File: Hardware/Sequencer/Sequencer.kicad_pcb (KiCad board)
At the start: 2 copper layers, 200 x 130 mm, 37 parts, among them J301 Conn_ST_STDC14, J601 USB_C_Receptacle_USB2.0_16P, SW301 SW_Push, SW401 SW_SP4T_NR01104, SW402 SW_SP4T_NR01104, SW403 SW_SP4T_NR01104, U301 STM32G474RETx, U401 MCP23017_SP, U402 MCP23017_SP, U601 USBLC6-2SC6, U602 AZ1117-3.3TRG1

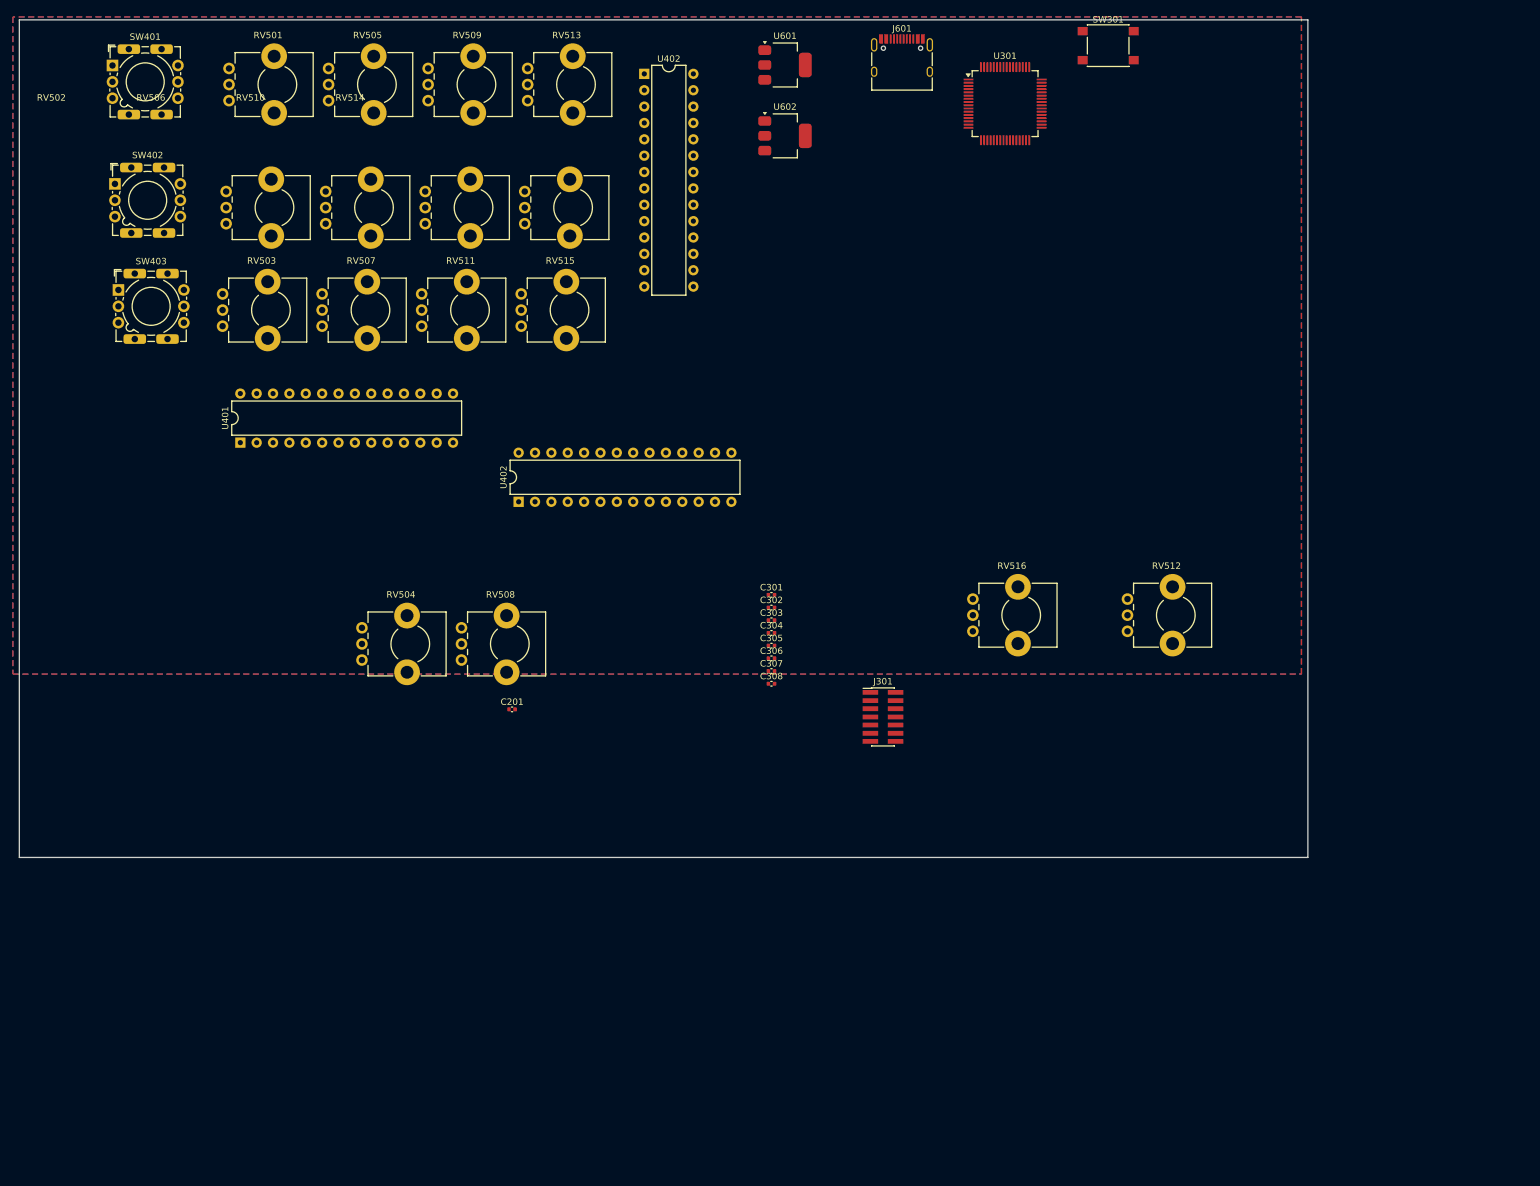
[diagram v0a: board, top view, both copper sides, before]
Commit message: update dimension pcb, footprint
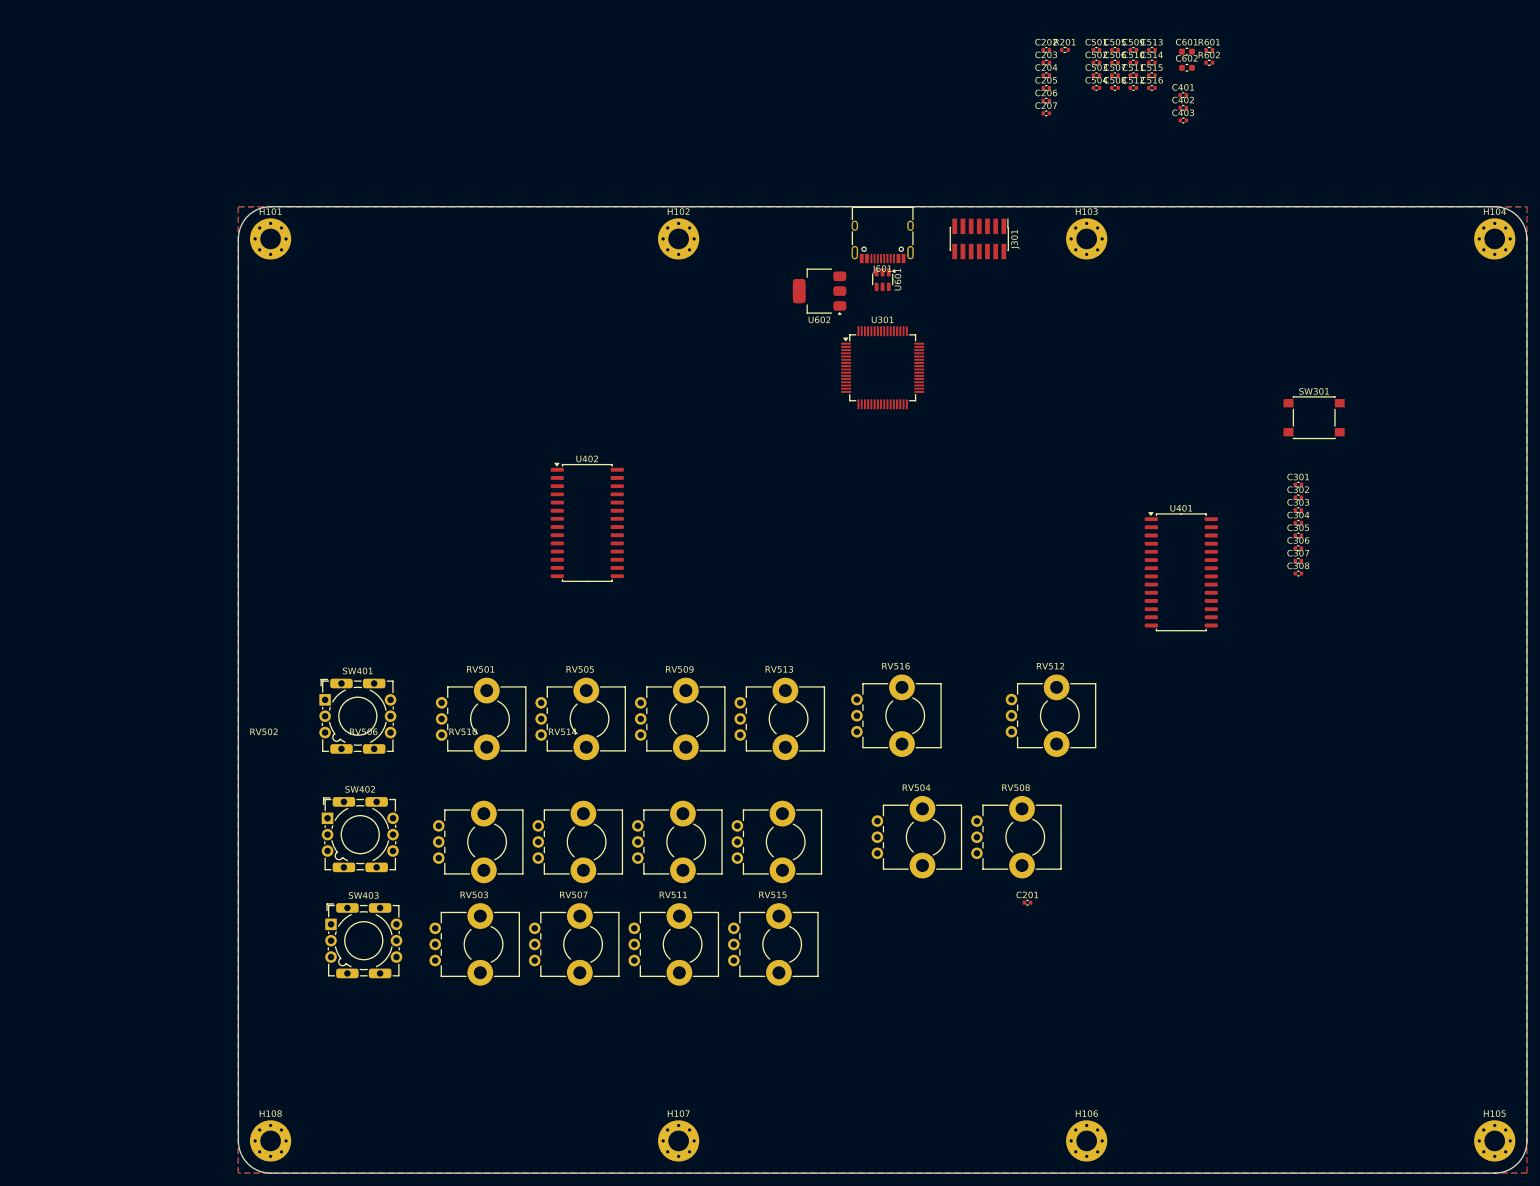
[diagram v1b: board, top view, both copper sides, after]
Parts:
- removed the U402 at (143.5, 95.8)
- added C202: 10n, Capacitor_SMD:C_0402_1005Metric, F.Cu at (225.4, 25.7)
- added C203: 1n, Capacitor_SMD:C_0402_1005Metric, F.Cu at (225.4, 27.6)
- added C204: 1n, Capacitor_SMD:C_0402_1005Metric, F.Cu at (225.4, 29.6)
- added C205: 1u, Capacitor_SMD:C_0402_1005Metric, F.Cu at (225.4, 31.6)
- added C206: 10n, Capacitor_SMD:C_0402_1005Metric, F.Cu at (225.4, 33.5)
- added C207: 1u, Capacitor_SMD:C_0402_1005Metric, F.Cu at (225.4, 35.5)
- added C401: 10n, Capacitor_SMD:C_0402_1005Metric, F.Cu at (246.7, 32.7)
- added C402: 10n, Capacitor_SMD:C_0402_1005Metric, F.Cu at (246.7, 34.6)
- added C403: 10n, Capacitor_SMD:C_0402_1005Metric, F.Cu at (246.7, 36.6)
- added C501: 10n, Capacitor_SMD:C_0402_1005Metric, F.Cu at (233.2, 25.7)
- added C502: 10n, Capacitor_SMD:C_0402_1005Metric, F.Cu at (233.2, 27.6)
- added C503: 10n, Capacitor_SMD:C_0402_1005Metric, F.Cu at (233.2, 29.6)
- added C504: 10n, Capacitor_SMD:C_0402_1005Metric, F.Cu at (233.2, 31.6)
- added C505: 10n, Capacitor_SMD:C_0402_1005Metric, F.Cu at (236.1, 25.7)
- added C506: 10n, Capacitor_SMD:C_0402_1005Metric, F.Cu at (236.1, 27.6)
- added C507: 10n, Capacitor_SMD:C_0402_1005Metric, F.Cu at (236.1, 29.6)
- added C508: 10n, Capacitor_SMD:C_0402_1005Metric, F.Cu at (236.1, 31.6)
- added C509: 10n, Capacitor_SMD:C_0402_1005Metric, F.Cu at (238.9, 25.7)
- added C510: 10n, Capacitor_SMD:C_0402_1005Metric, F.Cu at (238.9, 27.6)
- added C511: 10n, Capacitor_SMD:C_0402_1005Metric, F.Cu at (238.9, 29.6)
- added C512: 10n, Capacitor_SMD:C_0402_1005Metric, F.Cu at (238.9, 31.6)
- added C513: 10n, Capacitor_SMD:C_0402_1005Metric, F.Cu at (241.8, 25.7)
- added C514: 10n, Capacitor_SMD:C_0402_1005Metric, F.Cu at (241.8, 27.6)
- added C515: 10n, Capacitor_SMD:C_0402_1005Metric, F.Cu at (241.8, 29.6)
- added C516: 10n, Capacitor_SMD:C_0402_1005Metric, F.Cu at (241.8, 31.6)
- added C601: 10u, Capacitor_SMD:C_0603_1608Metric, F.Cu at (247.2, 25.9)
- added C602: 22u, Capacitor_SMD:C_0603_1608Metric, F.Cu at (247.2, 28.4)
- added H101: MountingHole_Pad, MountingHole:MountingHole_3.2mm_M3_Pad_Via, F.Cu at (105.0, 55.0)
- added H102: MountingHole_Pad, MountingHole:MountingHole_3.2mm_M3_Pad_Via, F.Cu at (168.3, 55.0)
- added H103: MountingHole_Pad, MountingHole:MountingHole_3.2mm_M3_Pad_Via, F.Cu at (231.7, 55.0)
- added H104: MountingHole_Pad, MountingHole:MountingHole_3.2mm_M3_Pad_Via, F.Cu at (295.0, 55.0)
- added H105: MountingHole_Pad, MountingHole:MountingHole_3.2mm_M3_Pad_Via, F.Cu at (295.0, 195.0)
- added H106: MountingHole_Pad, MountingHole:MountingHole_3.2mm_M3_Pad_Via, F.Cu at (231.7, 195.0)
- added H107: MountingHole_Pad, MountingHole:MountingHole_3.2mm_M3_Pad_Via, F.Cu at (168.3, 195.0)
- added H108: MountingHole_Pad, MountingHole:MountingHole_3.2mm_M3_Pad_Via, F.Cu at (105.0, 195.0)
- added R201: 1k, Resistor_SMD:R_0402_1005Metric, F.Cu at (228.3, 25.7)
- added R601: 5k1, Resistor_SMD:R_0402_1005Metric, F.Cu at (250.7, 25.7)
- added R602: 5k1, Resistor_SMD:R_0402_1005Metric, F.Cu at (250.7, 27.7)
- U401, U402: footprint Package_DIP:DIP-28_W7.62mm -> Package_SO:SOIC-28W_7.5x17.9mm_P1.27mm
- U601: footprint Package_TO_SOT_SMD:SOT-223-3_TabPin2 -> Package_TO_SOT_SMD:SOT-23-6
- moved U401 147.4 mm to (246.3, 106.7), turned to 0 degrees
- moved RV501 103.8 mm to (131.6, 132.0)
- moved RV505 103.8 mm to (147.0, 132.0)
- moved RV509 103.8 mm to (162.4, 132.0)
- moved RV513 103.8 mm to (177.9, 132.0)
- moved SW401 103.8 mm to (113.5, 126.5)
- moved RV502 103.8 mm to (131.1, 151.1)
- moved RV503 103.8 mm to (130.6, 167.0)
- moved RV506 103.8 mm to (146.6, 151.1)
- moved RV507 103.8 mm to (146.0, 167.0)
- moved RV510 103.8 mm to (162.0, 151.1)
- moved RV511 103.8 mm to (161.4, 167.0)
- moved RV514 103.8 mm to (177.4, 151.1)
- moved RV515 103.8 mm to (176.9, 167.0)
- moved SW403 103.8 mm to (114.4, 161.4)
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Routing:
- added copper zone on B.Cu, net GND
- added copper zone on F.Cu, net GND
- removed copper zone on B.Cu, net (none)
- removed copper zone on F.Cu, net (none)
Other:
- board size 200 x 130 mm -> 200 x 150 mm

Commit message: pcb
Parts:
- added C1: 100n, Capacitor_SMD:C_0402_1005Metric, B.Cu at (254.6, 137.1)
- added C10: 100n, Capacitor_SMD:C_0402_1005Metric, B.Cu at (134.2, 171.0)
- added C11: 100n, Capacitor_SMD:C_0402_1005Metric, F.Cu at (156.6, 166.1)
- added C12: 100n, Capacitor_SMD:C_0402_1005Metric, F.Cu at (176.6, 166.1)
- added C13: 100n, Capacitor_SMD:C_0402_1005Metric, F.Cu at (196.6, 166.1)
- added C14: 100n, Capacitor_SMD:C_0402_1005Metric, F.Cu at (216.6, 166.1)
- added C15: 100n, Capacitor_SMD:C_0402_1005Metric, F.Cu at (236.6, 166.1)
- added C16: 100n, Capacitor_SMD:C_0402_1005Metric, F.Cu at (256.6, 166.1)
- added C17: 100n, Capacitor_SMD:C_0402_1005Metric, F.Cu at (317.5, 135.0)
- added C2: 100n, Capacitor_SMD:C_0402_1005Metric, B.Cu at (234.1, 137.1)
- added C3: 100n, Capacitor_SMD:C_0402_1005Metric, B.Cu at (214.1, 137.1)
- added C4: 100n, Capacitor_SMD:C_0402_1005Metric, B.Cu at (194.1, 137.1)
- added C5: 100n, Capacitor_SMD:C_0402_1005Metric, B.Cu at (174.6, 137.1)
- added C6: 100n, Capacitor_SMD:C_0402_1005Metric, B.Cu at (154.1, 137.1)
- added C7: 100n, Capacitor_SMD:C_0402_1005Metric, B.Cu at (134.1, 137.1)
- added C8: 100n, Capacitor_SMD:C_0402_1005Metric, B.Cu at (114.1, 137.1)
- added C9: 100n, Capacitor_SMD:C_0402_1005Metric, B.Cu at (114.2, 171.0)
- added R1: 10k, Resistor_SMD:R_0402_1005Metric, F.Cu at (243.0, 139.3)
- added R10: 10k, Resistor_SMD:R_0402_1005Metric, B.Cu at (196.8, 142.8)
- added R12: 10k, Resistor_SMD:R_0402_1005Metric, F.Cu at (185.8, 141.6)
- added R13: 10k, Resistor_SMD:R_0402_1005Metric, B.Cu at (176.0, 142.8)
- added R15: 10k, Resistor_SMD:R_0402_1005Metric, F.Cu at (165.8, 141.6)
- added R16: 10k, Resistor_SMD:R_0402_1005Metric, B.Cu at (156.2, 143.0)
- added R18: 10k, Resistor_SMD:R_0402_1005Metric, F.Cu at (145.8, 141.6)
- added R19: 10k, Resistor_SMD:R_0402_1005Metric, B.Cu at (136.0, 142.3)
- added R21: 10k, Resistor_SMD:R_0402_1005Metric, F.Cu at (125.8, 141.6)
- added R22: 10k, Resistor_SMD:R_0402_1005Metric, B.Cu at (115.8, 142.5)
- added R24: 10k, Resistor_SMD:R_0402_1005Metric, F.Cu at (105.8, 141.6)
- added R25: 10k, Resistor_SMD:R_0402_1005Metric, F.Cu at (125.5, 169.5)
- added R27: 10k, Resistor_SMD:R_0402_1005Metric, F.Cu at (111.8, 165.2)
- added R28: 10k, Resistor_SMD:R_0402_1005Metric, F.Cu at (144.1, 166.6)
- added R3: 10k, Resistor_SMD:R_0402_1005Metric, F.Cu at (245.8, 141.6)
- added R30: 10k, Resistor_SMD:R_0402_1005Metric, F.Cu at (131.0, 185.5)
- added R31: 10k, Resistor_SMD:R_0402_1005Metric, F.Cu at (164.1, 166.6)
- added R33: 10k, Resistor_SMD:R_0402_1005Metric, F.Cu at (151.0, 186.2)
- added R34: 10k, Resistor_SMD:R_0402_1005Metric, F.Cu at (184.1, 166.6)
- added R36: 10k, Resistor_SMD:R_0402_1005Metric, F.Cu at (172.0, 186.8)
- added R37: 10k, Resistor_SMD:R_0402_1005Metric, F.Cu at (204.1, 166.6)
- added R39: 10k, Resistor_SMD:R_0402_1005Metric, F.Cu at (192.0, 187.8)
- added R4: 10k, Resistor_SMD:R_0402_1005Metric, B.Cu at (235.8, 142.2)
- added R40: 10k, Resistor_SMD:R_0402_1005Metric, F.Cu at (224.1, 166.6)
- added R42: 10k, Resistor_SMD:R_0402_1005Metric, F.Cu at (211.8, 188.5)
- added R43: 10k, Resistor_SMD:R_0402_1005Metric, F.Cu at (244.1, 166.6)
- added R45: 10k, Resistor_SMD:R_0402_1005Metric, F.Cu at (230.8, 189.2)
- added R46: 10k, Resistor_SMD:R_0402_1005Metric, F.Cu at (264.1, 166.6)
- added R48: 10k, Resistor_SMD:R_0402_1005Metric, F.Cu at (251.0, 190.2)
- added R6: 10k, Resistor_SMD:R_0402_1005Metric, F.Cu at (225.8, 141.6)
- added R7: 10k, Resistor_SMD:R_0402_1005Metric, B.Cu at (216.5, 142.8)
- added R9: 10k, Resistor_SMD:R_0402_1005Metric, F.Cu at (205.8, 141.6)
- added S1: 465M111172501, libs:465M111172501, F.Cu at (234.3, 132.6)
- added S10: 465M111172501, libs:465M111172501, F.Cu at (154.2, 175.6)
- added S11: 465M111172501, libs:465M111172501, F.Cu at (174.2, 175.6)
- added S12: 465M111172501, libs:465M111172501, F.Cu at (194.2, 175.6)
- added S13: 465M111172501, libs:465M111172501, F.Cu at (214.2, 175.6)
- added S14: 465M111172501, libs:465M111172501, F.Cu at (234.2, 175.6)
- added S15: 465M111172501, libs:465M111172501, F.Cu at (254.2, 175.6)
- added S2: 465M111172501, libs:465M111172501, F.Cu at (214.3, 132.6)
- added S3: 465M111172501, libs:465M111172501, F.Cu at (194.3, 132.6)
- added S4: 465M111172501, libs:465M111172501, F.Cu at (174.3, 132.6)
- added S401: 465M111172501, libs:465M111172501, F.Cu at (254.3, 132.6)
- added S5: 465M111172501, libs:465M111172501, F.Cu at (154.3, 132.6)
- added S6: 465M111172501, libs:465M111172501, F.Cu at (134.3, 132.6)
- added S7: 465M111172501, libs:465M111172501, F.Cu at (114.3, 132.6)
- added S8: 465M111172501, libs:465M111172501, F.Cu at (114.2, 175.6)
- added S9: 465M111172501, libs:465M111172501, F.Cu at (134.2, 175.6)
- added U1: PCA9635, Package_SO:TSSOP-28_4.4x9.7mm_P0.65mm, F.Cu at (126.1, 154.6)
- added U2: PCA9635, Package_SO:TSSOP-28_4.4x9.7mm_P0.65mm, F.Cu at (252.9, 154.6)
- added U4: MCP23017_SP, Package_SO:SOIC-28W_7.5x17.9mm_P1.27mm, F.Cu at (244.1, 101.2)
- U402: moved to B.Cu
- moved C506 156.4 mm to (85.8, 71.1)
- moved C507 156.4 mm to (85.8, 73.0)
- moved C508 156.4 mm to (85.8, 75.0)
- moved C502 156.4 mm to (83.0, 71.1)
- moved C503 156.4 mm to (83.0, 73.0)
- moved C504 156.4 mm to (83.0, 75.0)
- moved C509 156.4 mm to (88.7, 69.1)
- moved C510 156.4 mm to (88.7, 71.1)
- moved C511 156.4 mm to (88.7, 73.0)
- moved C512 156.4 mm to (88.7, 75.0)
- moved C513 156.4 mm to (91.6, 69.1)
- moved C514 156.4 mm to (91.6, 71.1)
- moved C515 156.4 mm to (91.6, 73.0)
- moved C516 156.4 mm to (91.6, 75.0)
- moved C501 150.3 mm to (86.5, 58.5), turned to -90 degrees
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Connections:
- net I2C_2_SCL renamed /STM32-G474RE/I2C_2_SCL
- net I2C_2_SDA renamed /STM32-G474RE/I2C_2_SDA
- U301 pad 10: ADC1_In8 -> /Potar/Voice2_Attack_pot
- U301 pad 11: ADC1_In9 -> /Potar/Voice2_Decay_pot
- U301 pad 12: ADC1_In1 -> /Potar/Pitch_octave_pot
- U301 pad 13: ADC1_In2 -> /Potar/Pitch_Main_pot
- U301 pad 14: ADC1_In3 -> /Potar/Voice1_PW_pot
- U301 pad 17: ADC1_In4 -> /Potar/Voice1_Attack_pot
- U301 pad 2: unconnected-(U301-PC13-Pad2) -> /MOS6581/A2
- U301 pad 20: ADC2_In3 -> /Potar/Voice3_Release_pot
- U301 pad 21: ADC2_In4 -> /Potar/Filter_Res_pot
- U301 pad 24: ADC1_In15 -> /Potar/Voice3_Decay_pot
- U301 pad 25: ADC1_In12 -> /Potar/Voice3_PW_pot
- U301 pad 26: unconnected-(U301-PB2-Pad26) -> /MOS6581/D0
- U301 pad 3: unconnected-(U301-PC14-Pad3) -> /MOS6581/A3
- U301 pad 33: ADC1_In14 -> /Potar/Voice3_Attack_pot
- U301 pad 34: ADC1_In11 -> /Potar/Voice2_Release_pot
- U301 pad 36: ADC1_In5 -> /Potar/Voice1_Decay_pot
- U301 pad 4: unconnected-(U301-PC15-Pad4) -> /MOS6581/A4
- U301 pad 40: I2C_3_SCL -> /GPIO_Expandeur/SDA Expandeur_Boutons
- U301 pad 41: I2C_3_SDA -> /GPIO_Expandeur/SCK Expandeur_Boutons
- U301 pad 45: /STM32-G474RE/USB_DM -> /PSU/USB_DM
- U301 pad 46: /STM32-G474RE/USB_DP -> /PSU/USB_DP
- U301 pad 49: I2C_1_SCL -> /GPIO_Expandeur/SCK LED_Driver
- U301 pad 50: I2C_1_SDA -> /GPIO_Expandeur/SDA LED_Driver
- U301 pad 53: unconnected-(U301-PC11-Pad53) -> /MOS6581/A0
- U301 pad 54: unconnected-(U301-PC12-Pad54) -> /MOS6581/A1
- U301 pad 56: unconnected-(U301-PB3-Pad56) -> /MOS6581/D1
- U301 pad 57: unconnected-(U301-PB4-Pad57) -> /MOS6581/D2
- U301 pad 58: unconnected-(U301-PB5-Pad58) -> /MOS6581/D3
- U301 pad 59: unconnected-(U301-PB6-Pad59) -> /MOS6581/D4
- U301 pad 6: /STM32-G474RE/ADC2_In10 -> /Potar/Filter_Freq_pot
- U301 pad 60: unconnected-(U301-PB7-Pad60) -> /MOS6581/D5
- U301 pad 61: unconnected-(U301-PB8-Pad61) -> /MOS6581/D6
- U301 pad 62: unconnected-(U301-PB9-Pad62) -> /MOS6581/D7
- U301 pad 8: ADC1_In6 -> /Potar/Voice1_Release_pot
- U301 pad 9: ADC1_In7 -> /Potar/Voice2_PW_pot
- U401 pad 12: unconnected-(U401-SCK-Pad12) -> /GPIO_Expandeur/SCK Expandeur_Boutons
- U401 pad 13: unconnected-(U401-SDA-Pad13) -> /GPIO_Expandeur/SDA Expandeur_Boutons
- U401 pad 18: unconnected-(U401-~{RESET}-Pad18) -> /GPIO_Expandeur/Reset
- U401 pad 19: unconnected-(U401-INTB-Pad19) -> /GPIO_Expandeur/INTA_Boutons
- U401 pad 20: unconnected-(U401-INTA-Pad20) -> /GPIO_Expandeur/INTB_Boutons
- U401 pad 25: unconnected-(U401-GPA4-Pad25) -> Net-(U401-GPA4)
- U401 pad 26: unconnected-(U401-GPA5-Pad26) -> Net-(U401-GPA5)
- U401 pad 27: unconnected-(U401-GPA6-Pad27) -> Net-(U401-GPA6)
- U401 pad 28: unconnected-(U401-GPA7-Pad28) -> Net-(U401-GPA7)
- U402 pad 12: unconnected-(U402-SCK-Pad12) -> Net-(U401-GPA5)
- U402 pad 13: unconnected-(U402-SDA-Pad13) -> Net-(U401-GPA4)
- U402 pad 18: unconnected-(U402-~{RESET}-Pad18) -> /GPIO_Expandeur/Reset
- U402 pad 19: unconnected-(U402-INTB-Pad19) -> Net-(U401-GPA6)
- U402 pad 20: unconnected-(U402-INTA-Pad20) -> Net-(U401-GPA7)
- U402 pad 21: /GPIO_Expandeur/A0 -> /GPIO_Expandeur/B8
- U402 pad 22: /GPIO_Expandeur/A1 -> /GPIO_Expandeur/B9
- U402 pad 23: /GPIO_Expandeur/A2 -> /GPIO_Expandeur/B10
- U402 pad 24: /GPIO_Expandeur/A3 -> /GPIO_Expandeur/B11
- U402 pad 25: /GPIO_Expandeur/A4 -> /GPIO_Expandeur/B12
- U402 pad 26: /GPIO_Expandeur/A5 -> /GPIO_Expandeur/B13
- U402 pad 27: /GPIO_Expandeur/A6 -> /GPIO_Expandeur/B14
- U402 pad 28: /GPIO_Expandeur/A7 -> /GPIO_Expandeur/B15
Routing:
- net /GPIO_Expandeur/B15_B: track 0.00 -> 209.1 mm
- net /GPIO_Expandeur/B14_B: track 0.00 -> 188.3 mm
- net /GPIO_Expandeur/B13_B: track 0.00 -> 168.4 mm
- net /GPIO_Expandeur/B8: track 0.00 -> 158.8 mm
- net /GPIO_Expandeur/B12_B: track 0.00 -> 148.4 mm
- net /GPIO_Expandeur/B7_R: track 0.00 -> 142.2 mm, vias 0 -> 1
- net /GPIO_Expandeur/B0_B: track 0.00 -> 140.5 mm
- net /GPIO_Expandeur/B8_R: track 0.00 -> 139.0 mm
- net /GPIO_Expandeur/B11_B: track 0.00 -> 127.8 mm
- net /GPIO_Expandeur/B1_B: track 0.00 -> 127.2 mm
- net /GPIO_Expandeur/B9_R: track 0.00 -> 120.5 mm
- net /GPIO_Expandeur/B6_R: track 0.00 -> 120.3 mm, vias 0 -> 1
- net /GPIO_Expandeur/B2_B: track 0.00 -> 110.9 mm
- net /GPIO_Expandeur/B10_B: track 0.00 -> 105.8 mm
- net /GPIO_Expandeur/B10_R: track 0.00 -> 102.4 mm
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- added copper zone on In1.Cu, net +3.3V
- added copper zone on In2.Cu, net GND
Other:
- copper layers 2 -> 4

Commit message: PCB PCB
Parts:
- C11: moved to B.Cu
- moved RV502 12.8 mm to (137.8, 67.0), turned to 180 degrees
- moved RV503 12.8 mm to (153.8, 67.0), turned to 180 degrees
- moved RV504 12.8 mm to (169.8, 67.0), turned to 180 degrees
- moved RV506 12.8 mm to (137.8, 85.0), turned to 180 degrees
- moved RV507 12.8 mm to (153.8, 85.0), turned to 180 degrees
- moved RV508 12.8 mm to (169.8, 85.0), turned to 180 degrees
- moved RV512 12.8 mm to (137.8, 103.0), turned to 180 degrees
- moved RV513 12.8 mm to (153.8, 103.0), turned to 180 degrees
- moved RV515 12.8 mm to (169.8, 103.0), turned to 180 degrees
- moved RV501 12.3 mm to (121.3, 67.0), turned to 180 degrees
- moved RV505 12.3 mm to (121.3, 85.0), turned to 180 degrees
- moved RV510 12.3 mm to (121.3, 103.0), turned to 180 degrees
- moved U1 3.43 mm to (122.8, 155.2), turned to 90 degrees
- turned C10 to 180 degrees
- turned C11 to 0 degrees
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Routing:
- net /GPIO_Expandeur/B15_B: track 209.1 -> 0.00 mm
- net /GPIO_Expandeur/B14_B: track 188.3 -> 0.00 mm
- net /GPIO_Expandeur/B13_B: track 168.4 -> 0.00 mm
- net /GPIO_Expandeur/B12_B: track 148.4 -> 0.00 mm
- net /GPIO_Expandeur/B7_R: track 142.2 -> 0.00 mm, vias 1 -> 0
- net /GPIO_Expandeur/B8: track 158.8 -> 18.4 mm
- net /GPIO_Expandeur/B0_B: track 140.5 -> 7.91 mm
- net /GPIO_Expandeur/B1_B: track 127.2 -> 0.00 mm
- net /GPIO_Expandeur/B11_B: track 127.8 -> 0.60 mm
- net /GPIO_Expandeur/B8_R: track 139.0 -> 18.7 mm
- net /GPIO_Expandeur/B6_R: track 120.3 -> 3.02 mm, vias 1 -> 0
- net /GPIO_Expandeur/B9_R: track 120.5 -> 7.38 mm
- net /GPIO_Expandeur/B2_B: track 110.9 -> 0.00 mm
- net /GPIO_Expandeur/B10_B: track 105.8 -> 0.03 mm
- net /GPIO_Expandeur/B5_R: track 99.3 -> 0.00 mm, vias 1 -> 0
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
